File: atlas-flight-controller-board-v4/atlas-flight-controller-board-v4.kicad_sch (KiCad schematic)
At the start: 0 parts

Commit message: Sensor schematics done.
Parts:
- added U1: STM32F405RG, STM32F405RG:ST_LQFP64, symbol STM32F405RG:STM32F405RG
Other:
- added sheet sensors (sensors.kicad_sch)

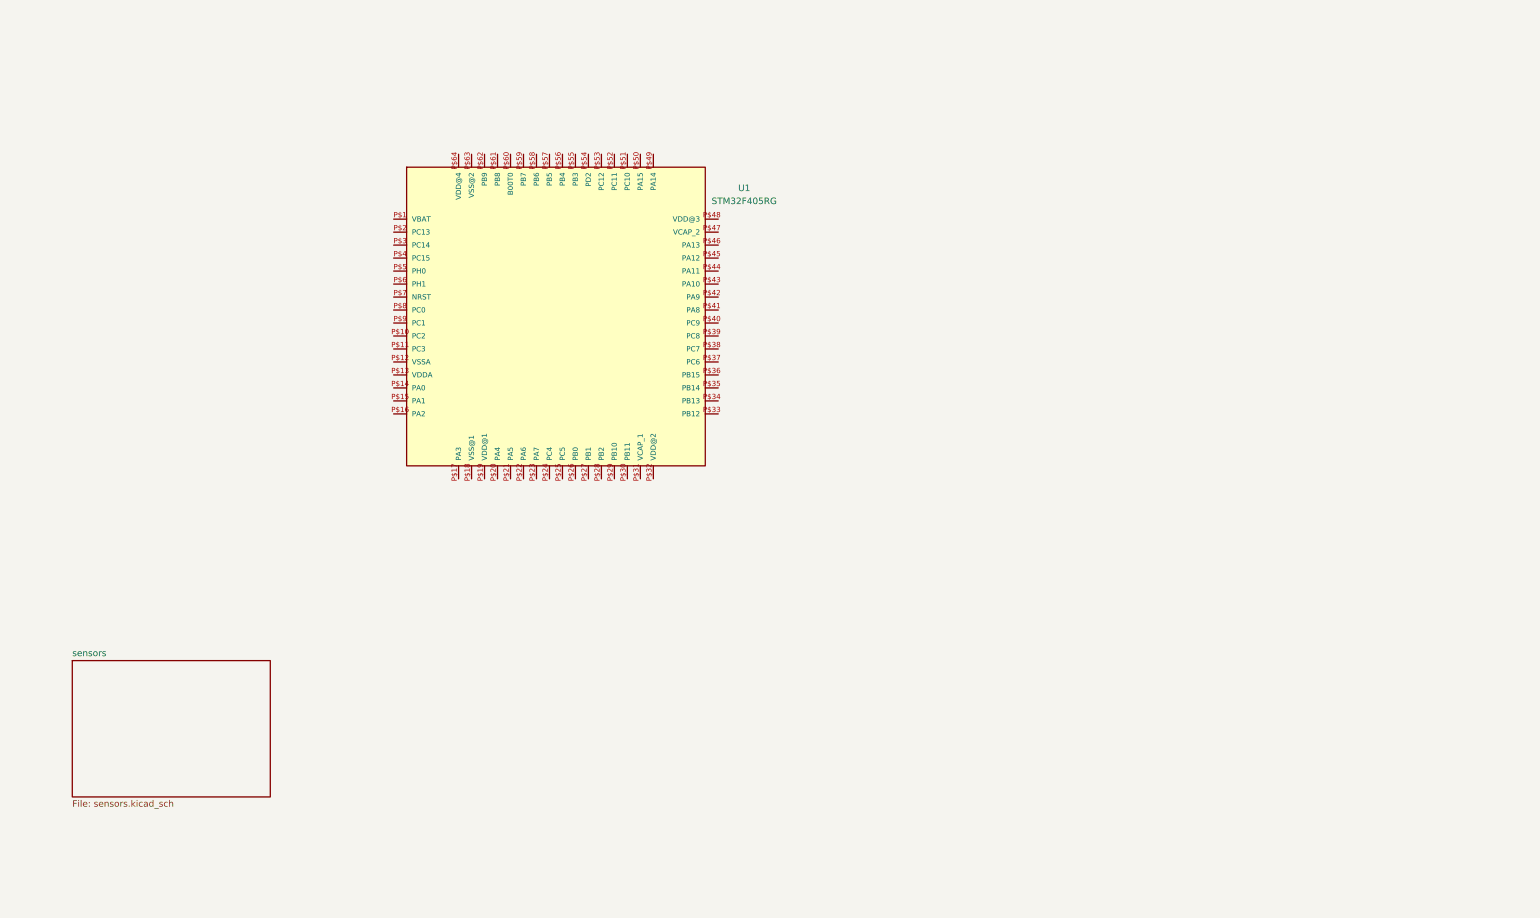
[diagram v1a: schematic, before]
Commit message: Configured boot pin, power and gnd, decoupling and filtering for analog 3v3.
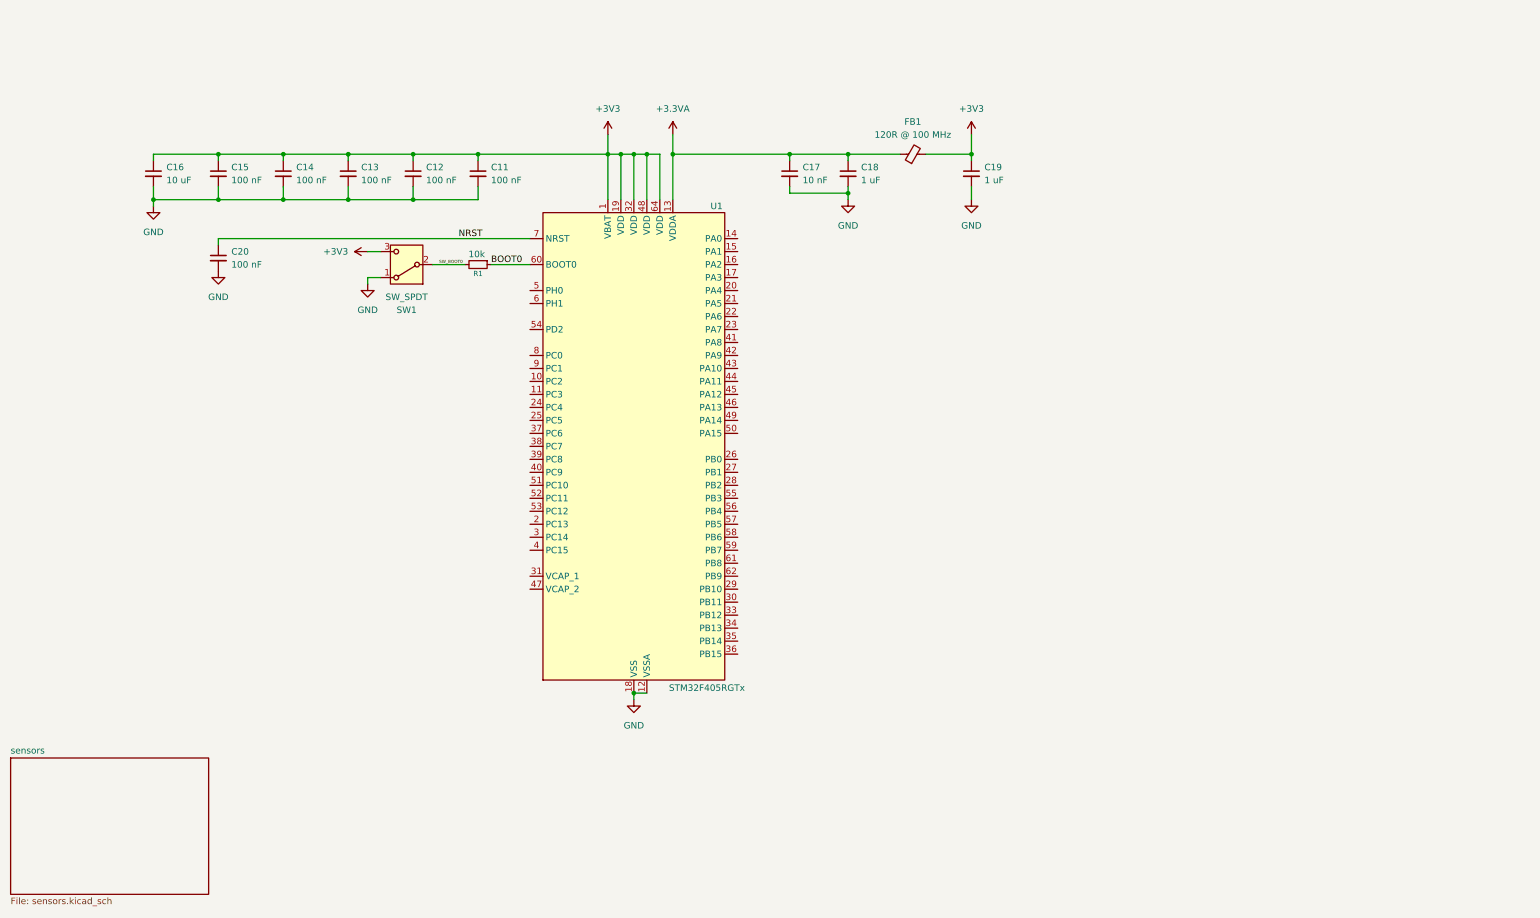
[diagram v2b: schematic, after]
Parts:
- removed U1: STM32F405RG, STM32F405RG:ST_LQFP64, symbol STM32F405RG:STM32F405RG
- added C11, C12, C13, C14, C15, C20: 100 nF, Capacitor_SMD:C_0603_1608Metric_Pad1.08x0.95mm_HandSolder, symbol Device:C_Small
- added C16: 10 uF, Capacitor_SMD:C_0603_1608Metric_Pad1.08x0.95mm_HandSolder, symbol Device:C_Small
- added C17: 10 nF, Capacitor_SMD:C_0603_1608Metric_Pad1.08x0.95mm_HandSolder, symbol Device:C_Small
- added C18, C19: 1 uF, Capacitor_SMD:C_0603_1608Metric_Pad1.08x0.95mm_HandSolder, symbol Device:C_Small
- added FB1: 120R @ 100 MHz, symbol Device:FerriteBead_Small
- added R1: 10k, Resistor_SMD:R_0603_1608Metric_Pad0.98x0.95mm_HandSolder, symbol Device:R_Small
- added SW1: SW_SPDT, symbol Switch:SW_SPDT
- added U1: STM32F405RGTx, Package_QFP:LQFP-64_10x10mm_P0.5mm, symbol MCU_ST_STM32F4:STM32F405RGTx
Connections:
- new net +3.3VA: C17.1, C18.1, FB1.1, U1.13 (VDDA)
- new net +3V3: C11.1, C12.1, C13.1, C14.1, C15.1, C16.1, C19.1, FB1.2, SW1.3 (C), U1.1 (VBAT), U1.19 (VDD), U1.32 (VDD), U1.48 (VDD), U1.64 (VDD)
- new net BOOT0: R1.1, U1.60 (BOOT0)
- new net GND: C11.2, C12.2, C13.2, C14.2, C15.2, C16.2, C17.2, C18.2, C19.2, C20.2, SW1.1 (A), U1.12 (VSSA), U1.18 (VSS), U1.63 (VSS)
- new net NRST: C20.1, U1.7 (NRST)
- new net SW_BOOT0: R1.2, SW1.2 (B)

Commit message: Added stuff
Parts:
- added C21, C22: 10 pF, Capacitor_SMD:C_0603_1608Metric_Pad1.08x0.95mm_HandSolder, symbol Device:C_Small
- added J1: DX07S016JA1R1500, usb-c:JAE_DX07S016JA1R1500, symbol usb-c:DX07S016JA1R1500
- added Y1: 16 MHz, Crystal:Crystal_SMD_3225-4Pin_3.2x2.5mm_HandSoldering, symbol Device:Crystal_GND24
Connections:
- net GND: now also C21.2, C22.2, J1.1 (GND), J1.12 (GND), J1.S1 (SHIELD), J1.S2 (SHIELD), J1.S3 (SHIELD), J1.S4 (SHIELD), J1.S5 (SHIELD), J1.S6 (SHIELD), Y1.2, Y1.4
- net SWDIO: now reaches U1.46 (PA13)
- net SWCLK: now reaches U1.49 (PA14)
- net HSE_IN: now reaches U1.5 (PH0)
- net HSE_IN: now also C21.1, Y1.1
- net HSE_OUT: now reaches U1.6 (PH1)
- net HSE_OUT: now also C22.1, Y1.3
- new net: J1.5 (D-), J1.8 (D-)
- new net: J1.6 (D+), J1.7 (D+)
- new net VBUS: J1.11 (VBUS), J1.2 (VBUS)
- no-connect marks 0 -> 2
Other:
- note added: "NEED ESD PROTECTION AND VBUS VOLTAGE DIV"
- moved on the sheet: R1, SW1

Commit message: commiting files to v10 branch. Only v9 is working well on linux so seperating to reduce headache while sorting out issues
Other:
- added sheet power (power.kicad_sch)
- added sheet radio (radio.kicad_sch)
- added sheet sd-card (sd-card.kicad_sch)
- note added: "NEEDS TO HAVE PYRO CHANNEL"
- company: (none) -> Sam Manley, ARCUIA
- title: (none) -> Atlas v4 Flight Controller

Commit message: wip commit, hopefully last from mac
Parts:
- added C40: 100nF, Capacitor_SMD:C_0603_1608Metric, symbol Device:C_Small
- added H1, H2, H3, H4: MountingHole, MountingHole:MountingHole_2.2mm_M2_Pad_Via, symbol Mechanical:MountingHole
- added J5: Conn_ARM_SWD_TagConnect_TC2030-NL, Connector:Tag-Connect_TC2030-IDC-NL_2x03_P1.27mm_Vertical, symbol Connector:Conn_ARM_SWD_TagConnect_TC2030-NL
- added R17, R18: 10k, Resistor_SMD:R_0603_1608Metric, symbol Device:R_Small
- added R4: 33k, Resistor_SMD:R_0603_1608Metric, symbol Device:R_Small
- added R5: 82k, Resistor_SMD:R_0603_1608Metric, symbol Device:R_Small
- added R6, R7: 5k1, Resistor_SMD:R_0603_1608Metric, symbol Device:R_Small
- added SW2: SW_SPDT, symbol Switch:SW_SPDT
- added SW3: SW_Push, symbol Switch:SW_Push
- added U9: USBLC6, Package_TO_SOT_SMD:SOT-666, symbol Power_Protection:USBLC6-2P6
- C11, C12, C13, C14, C15, C16, C17, C18, C19, C20, C21, C22: footprint Capacitor_SMD:C_0603_1608Metric_Pad1.08x0.95mm_HandSolder -> Capacitor_SMD:C_0603_1608Metric
- R1: footprint Resistor_SMD:R_0603_1608Metric_Pad0.98x0.95mm_HandSolder -> Resistor_SMD:R_0603_1608Metric
- Y1: footprint Crystal:Crystal_SMD_3225-4Pin_3.2x2.5mm_HandSoldering -> Crystal:Crystal_SMD_3225-4Pin_3.2x2.5mm
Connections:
- net +3V3: now also J5.1 (VCC), SW2.3 (C)
- net GND: now also C40.1, J5.5 (GND), R5.1, R6.1, R7.1, SW2.1 (A), SW3.2, U9.2 (GND)
- net NRST: now also J5.3 (~{RESET})
- net SWCLK: now also J5.4 (SWCLK)
- net SWDIO: now also J5.2 (SWDIO)
- net USB_DP+: now also J1.6 (D+), J1.7 (D+), U1.45 (PA12), U9.3 (I/O2), U9.4 (I/O2)
- net USB_DP-: now also J1.5 (D-), J1.8 (D-), U1.44 (PA11), U9.1 (I/O1), U9.6 (I/O1)
- net VBUS: now also R4.2, U9.5 (VBUS)
- net VBUS_SENSE: now also U1.42 (PA9), R4.1, R5.2
- net at J1.3 (CC1): now also R6.2
- net at J1.9 (CC2): now also R7.2
- net CS_LORA: now reaches U1.20 (PA4)
- net SCK_LORA: now reaches U1.21 (PA5)
- net MISO_LORA: now reaches U1.22 (PA6)
- net MOSI_LORA: now reaches U1.23 (PA7)
- net at U1.28 (PB2): now also R17.1
- net SCK_MEMS: now reaches U1.34 (PB13)
- net MISO_MEMS: now reaches U1.35 (PB14)
- net MOSI_MEMS: now reaches U1.36 (PB15)
- net CS_FLASH: now reaches U1.50 (PA15)
- net SCK_FLASH: now reaches U1.51 (PC10)
- net MISO_FLASH: now reaches U1.52 (PC11)
- net MOSI_FLASH: now reaches U1.53 (PC12)
- net SWO: now reaches U1.55 (PB3)
- net SWO: now also J5.6 (SWO)
- new net: C40.2, R18.2, SW3.1
- new net STANDBY_TOGGLE: R18.1
- new net SW_BOOT1: R17.2, SW2.2 (B)
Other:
- note added: "NEED TO HAVE POWER SWITCHES, 1 FOR MOTORS, 1 FOR CAMERAS"
- note added: "NEEDS PWM CHANNELS X4"
- note added: "NEEDS TO HAVE CONNECTOR FOR EXTERNAL I2C BUS (THAT TIES INTO ONBOARD CURRENT SENSING)"
- note removed: "NEED ESD PROTECTION AND VBUS VOLTAGE DIV"
- moved on the sheet: J1

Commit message: schematic done mostly besides style and footprints
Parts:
- removed C11, C12, C13, C14, C15, C20: 100 nF, Capacitor_SMD:C_0603_1608Metric, symbol Device:C_Small
- removed C16: 10 uF, Capacitor_SMD:C_0603_1608Metric, symbol Device:C_Small
- removed C17: 10 nF, Capacitor_SMD:C_0603_1608Metric, symbol Device:C_Small
- removed C18, C19: 1 uF, Capacitor_SMD:C_0603_1608Metric, symbol Device:C_Small
- removed C21, C22: 10 pF, Capacitor_SMD:C_0603_1608Metric, symbol Device:C_Small
- removed C40: 100nF, Capacitor_SMD:C_0603_1608Metric, symbol Device:C_Small
- removed FB1: 120R @ 100 MHz, symbol Device:FerriteBead_Small
- removed H1, H2, H3, H4: MountingHole, MountingHole:MountingHole_2.2mm_M2_Pad_Via, symbol Mechanical:MountingHole
- removed J1: DX07S016JA1R1500, usb-c:JAE_DX07S016JA1R1500, symbol usb-c:DX07S016JA1R1500
- removed J5: Conn_ARM_SWD_TagConnect_TC2030-NL, Connector:Tag-Connect_TC2030-IDC-NL_2x03_P1.27mm_Vertical, symbol Connector:Conn_ARM_SWD_TagConnect_TC2030-NL
- removed R1, R17, R18: 10k, Resistor_SMD:R_0603_1608Metric, symbol Device:R_Small
- removed R4: 33k, Resistor_SMD:R_0603_1608Metric, symbol Device:R_Small
- removed R5: 82k, Resistor_SMD:R_0603_1608Metric, symbol Device:R_Small
- removed R6, R7: 5k1, Resistor_SMD:R_0603_1608Metric, symbol Device:R_Small
- removed SW1, SW2: SW_SPDT, symbol Switch:SW_SPDT
- removed SW3: SW_Push, symbol Switch:SW_Push
- removed U1: STM32F405RGTx, Package_QFP:LQFP-64_10x10mm_P0.5mm, symbol MCU_ST_STM32F4:STM32F405RGTx
- removed U9: USBLC6, Package_TO_SOT_SMD:SOT-666, symbol Power_Protection:USBLC6-2P6
- removed Y1: 16 MHz, Crystal:Crystal_SMD_3225-4Pin_3.2x2.5mm, symbol Device:Crystal_GND24
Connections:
- no-connect marks 2 -> 0
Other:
- added sheet stm32 (stm32.kicad_sch)
- note removed: "NEED TO HAVE POWER SWITCHES, 1 FOR MOTORS, 1 FOR CAMERAS"
- note removed: "NEEDS PWM CHANNELS X4"
- note removed: "NEEDS TO HAVE CONNECTOR FOR EXTERNAL I2C BUS (THAT TIES INTO ONBOARD CURRENT SENSING)"
- note removed: "NEEDS TO HAVE PYRO CHANNEL"

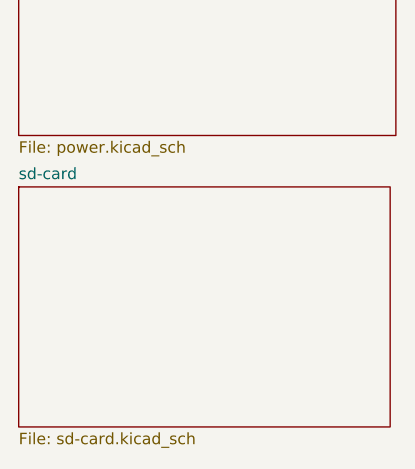
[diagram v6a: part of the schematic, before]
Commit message: progress update. schematic has been done, layout is half finished. board is now 50x65mm for rf performance reasons
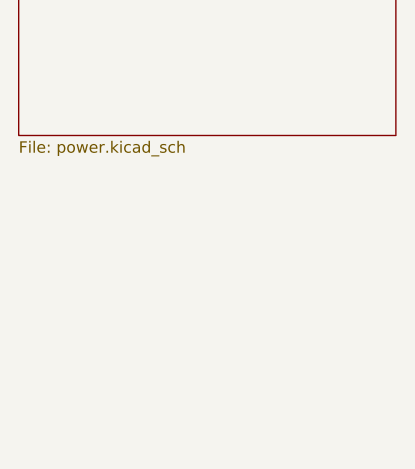
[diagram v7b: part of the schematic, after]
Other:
- removed sheet sd-card
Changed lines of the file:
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@@
-	)
-	(sheet
-		(at 19.05 149.86)
-		(size 41.275 26.67)
-		(exclude_from_sim no)
-		(in_bom yes)
-		(on_board yes)
-		(dnp no)
-		(fields_autoplaced yes)
-		(stroke
-			(width 0.1524)
-			(type solid)
-		)
-		(fill
-			(color 0 0 0 0)
-		)
-		(property "Sheetname" "sd-card"
-			(at 19.05 149.1484 0)
-			(show_name no)
-			(do_not_autoplace no)
-			(effects
-				(font
-					(size 1.27 1.27)
-				)
-				(justify left bottom)
-			)
-		)
-		(property "Sheetfile" "sd-card.kicad_sch"
-			(at 19.05 177.1146 0)
-			(show_name no)
-			(do_not_autoplace no)
-			(effects
-				(font
-					(size 1.27 1.27)
-				)
-				(justify left top)
-			)
-		)
-		(instances
-			(project "atlas-flight-controller-board-v4"
-				(path "/5e529273-3bf8-4f62-b3e5-dd579b5c7f6d"
-					(page "4")
-				)
-			)
-		)
 	)
 	(sheet
@@
 			(project "atlas-flight-controller-board-v4"
 				(path "/5e529273-3bf8-4f62-b3e5-dd579b5c7f6d"
-					(page "6")
+					(page "2")
 				)
 			)
@@
 			(project "atlas-flight-controller-board-v4"
 				(path "/5e529273-3bf8-4f62-b3e5-dd579b5c7f6d"
-					(page "3")
+					(page "4")
 				)
 			)
@@
 			(project "atlas-flight-controller-board-v4"
 				(path "/5e529273-3bf8-4f62-b3e5-dd579b5c7f6d"
-					(page "2")
+					(page "3")
 				)
 			)
